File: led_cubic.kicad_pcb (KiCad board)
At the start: 2 copper layers, 100 x 100 mm, 82 parts, among them J1 Cathode Layer, Q1 2N2222, Q2 2N2222, Q3 2N2222, Q4 2N2222, U1 74HC595, U2 74HC595, U3 74HC595, U4 74HC595, U5 74HC595, U6 74HC595, U7 74HC595, U8 CORE-ESP32-C3-DevKit

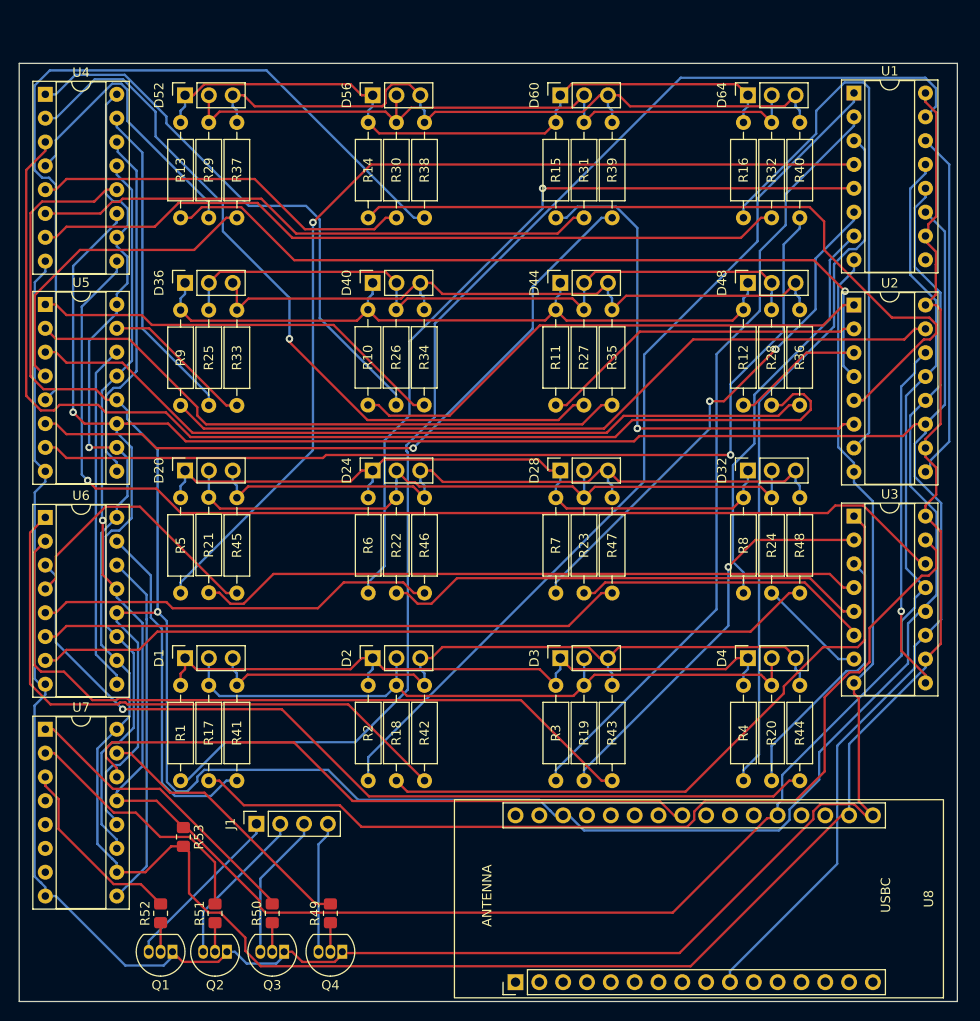
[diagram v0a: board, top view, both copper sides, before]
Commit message: 0.1.1
修改布局和PCB大小并添加M3螺丝孔
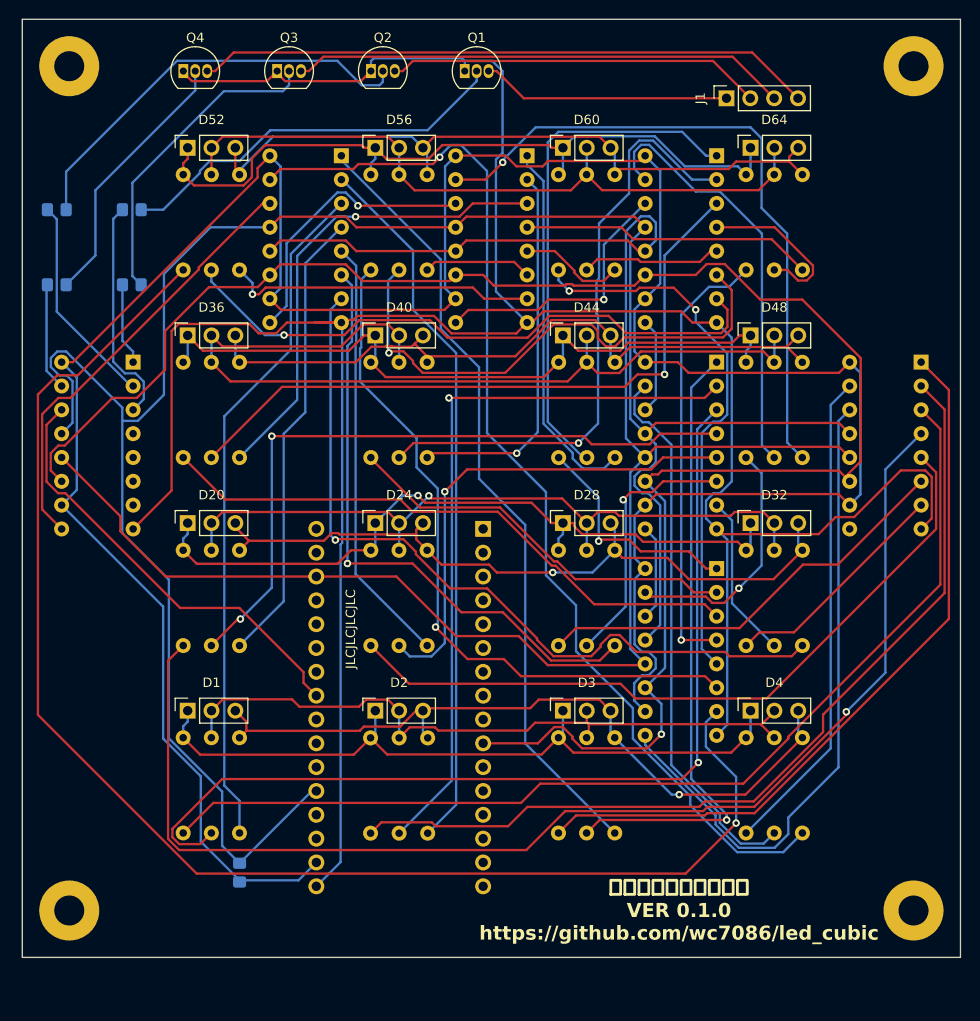
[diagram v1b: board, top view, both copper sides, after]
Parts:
- added P1: MountingHole_3.2mm_M3_Pad, MountingHole:MountingHole_3.2mm_M3_Pad, F.Cu at (183.4, 134.5)
- added P2: MountingHole_3.2mm_M3_Pad, MountingHole:MountingHole_3.2mm_M3_Pad, F.Cu at (93.4, 134.5)
- added P3: MountingHole_3.2mm_M3_Pad, MountingHole:MountingHole_3.2mm_M3_Pad, F.Cu at (93.4, 44.5)
- added P4: MountingHole_3.2mm_M3_Pad, MountingHole:MountingHole_3.2mm_M3_Pad, F.Cu at (183.4, 44.5)
- J1: footprint Connector_PinSocket_2.54mm:PinSocket_1x04_P2.54mm_Vertical -> Library:PinSocket_1x04_P2.54mm_Vertical
- R1, R10, R11, R12, R13, R14, R15, R16, R17, R18, R19, R2, R20, R21, R22, R23, R24, R25, R26, R27, R28, R29, R3, R30, R31, R32, R33, R34, R35, R36, R37, R38, R39, R4, R40, R41, R42, R43, R44, R45, R46, R47, R48, R49, R5, R50, R51, R52, R53, R6, R7, R8, R9, U8: moved to B.Cu
- U1, U2, U3, U4, U5, U6, U7: footprint Package_DIP:DIP-16_W7.62mm_Socket -> Library:DIP-16_W7.62mm_Socket; moved to B.Cu
- moved Q1 98.9 mm to (135.6, 45.1), turned to 0 degrees
- moved Q4 95.4 mm to (105.6, 45.1), turned to 0 degrees
- moved Q2 95.1 mm to (125.6, 45.1), turned to 0 degrees
- moved Q3 93.9 mm to (115.6, 45.1), turned to 0 degrees
- moved J1 92.2 mm to (163.5, 48.0)
- moved R51 76.9 mm to (92.1, 59.8), turned to 180 degrees
- moved R52 75.1 mm to (100.1, 59.8), turned to 180 degrees
- moved R49 73.1 mm to (92.1, 67.8), turned to 180 degrees
- moved R50 68.7 mm to (100.1, 67.8), turned to 180 degrees
- moved U4 68.0 mm to (158.6, 53.8), turned to 180 degrees
- moved R1 60.5 mm to (165.6, 116.1)
- moved R17 60.5 mm to (168.6, 116.1)
- moved R41 60.5 mm to (171.6, 116.1)
- moved R13 60.5 mm to (165.6, 56.1)
- moved R29 60.5 mm to (168.6, 56.1)
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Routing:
- net Net-(U3-SER): track 118.8 -> 10.2 mm, vias 1 -> 0
- net Net-(U2-QH): track 60.8 -> 152.5 mm, vias 0 -> 1
- net Net-(U1-QA): track 136.8 -> 52.2 mm
- net Net-(U6-QA): track 37.0 -> 117.3 mm, vias 0 -> 1
- net Net-(U3-QD): track 28.4 -> 103.3 mm, vias 0 -> 1
- net Net-(U5-QF): track 84.1 -> 11.3 mm
- net Net-(U5-QH): track 102.0 -> 33.2 mm
- net /P10: track 262.1 -> 194.2 mm
- net /P19: track 260.6 -> 192.9 mm, vias 1 -> 0
- net Net-(U5-QG): track 74.3 -> 11.6 mm, vias 1 -> 0
- net GND: track 237.3 -> 295.9 mm
- net Net-(U2-QA): track 84.8 -> 26.7 mm, vias 0 -> 1
- net Net-(U5-QA): track 16.2 -> 71.4 mm, vias 0 -> 1
- net /GND4: track 14.1 -> 65.8 mm
- net Net-(U2-QD): track 14.1 -> 63.9 mm
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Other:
- board text added: "JLCJLCJLCJLC"
- board text added: "陈基城，高鑫，覃远明 VER 0.1.0 https://github.com/wc7086/led_cubic"

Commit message: 0.1.2
调整 LED 插座焊盘间距，修改布局，重新布线
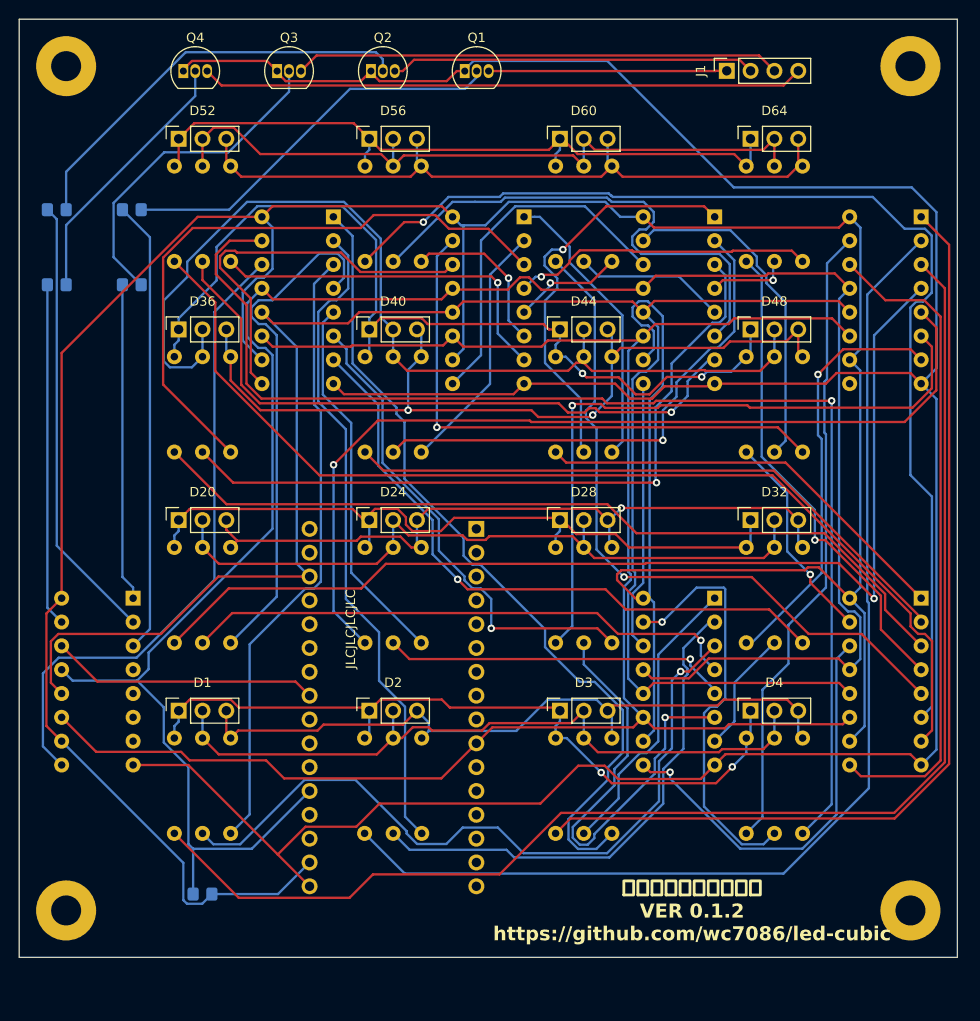
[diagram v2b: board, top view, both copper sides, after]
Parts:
- moved U3 25.2 mm to (158.4, 100.9)
- moved U7 25.2 mm to (96.4, 100.9)
- moved U2 22.0 mm to (180.4, 100.9)
- moved U1 15.5 mm to (180.4, 60.3)
- moved U6 6.57 mm to (117.8, 60.3)
- moved U5 6.52 mm to (138.1, 60.3)
- moved U4 6.51 mm to (158.4, 60.3)
- moved R53 4.57 mm to (107.6, 132.8), turned to 0 degrees
- moved J1 2.93 mm to (163.5, 45.0)
- moved D52 1.36 mm to (105.1, 52.3)
- moved R16 1.31 mm to (104.6, 55.2)
- moved R32 1.31 mm to (107.6, 55.2)
- moved R40 1.31 mm to (110.6, 55.2)
- moved D36 1.15 mm to (105.1, 72.6)
- moved D56 1.15 mm to (125.4, 52.3)
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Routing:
- net +5V: track 292.4 -> 356.1 mm
- net Net-(U2-QG): track 74.7 -> 119.4 mm
- net Net-(U2-QH): track 152.5 -> 113.8 mm, vias 1 -> 0
- net Net-(U3-QB): track 67.0 -> 31.3 mm, vias 1 -> 0
- net Net-(U2-SER): track 10.2 -> 44.8 mm, vias 0 -> 1
- net Net-(U1-QD): track 111.3 -> 145.1 mm
- net Net-(U1-QG): track 45.9 -> 71.7 mm, vias 0 -> 1
- net Net-(U2-QD): track 63.9 -> 89.2 mm
- net Net-(U7-QB): track 8.72 -> 33.9 mm
- net Net-(U7-QA): track 11.5 -> 36.6 mm
- net Net-(U7-QC): track 22.7 -> 47.7 mm
- net Net-(U1-QB): track 79.7 -> 104.6 mm
- net Net-(U3-QD): track 103.3 -> 78.7 mm
- net Net-(U7-QD): track 24.2 -> 48.4 mm
- net Net-(U2-QC): track 42.9 -> 67.0 mm
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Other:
- board text added: "陈基城，高鑫，覃远明 VER 0.1.2 https://github.com/wc7086/led-cubic"
- board text removed: "陈基城，高鑫，覃远明 VER 0.1.0 https://github.com/wc7086/led_cubic"

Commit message: 修复PCB，删除每排LED的并联线路
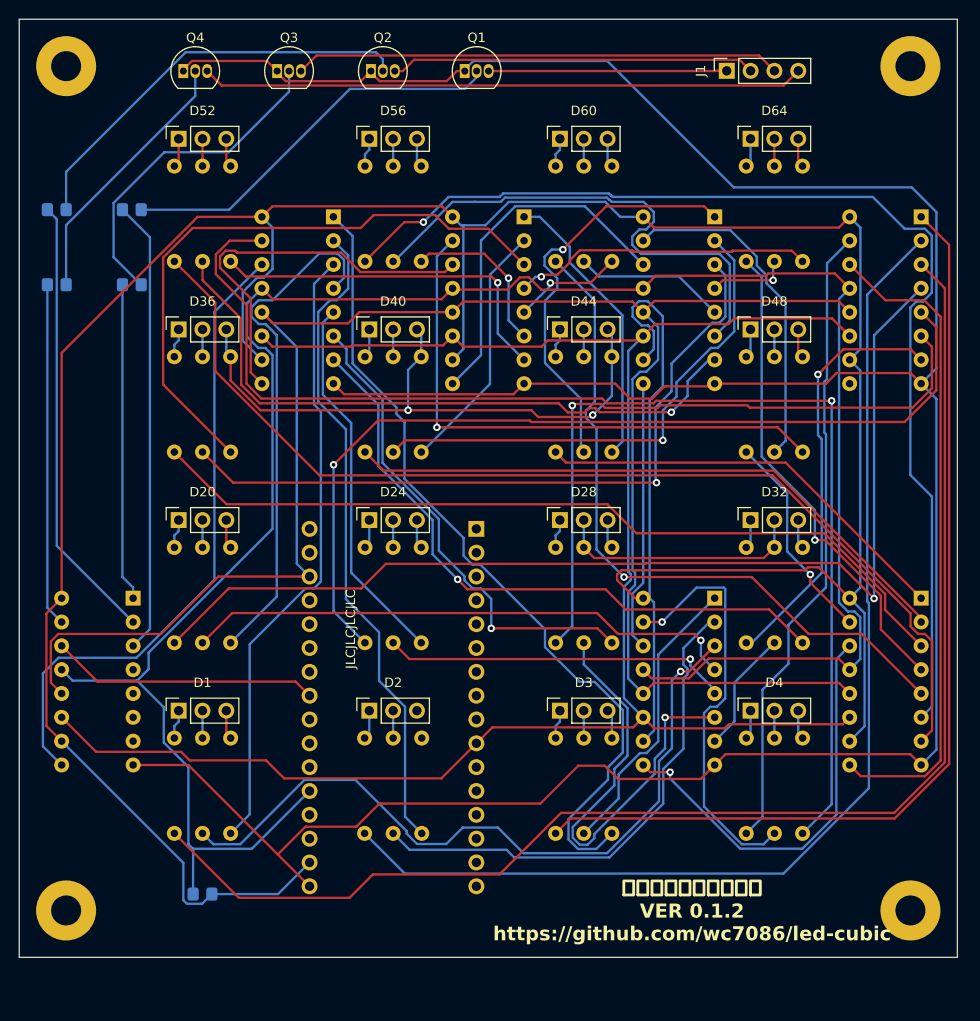
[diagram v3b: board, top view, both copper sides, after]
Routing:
- net /G3: track 106.6 -> 11.6 mm
- net /B3: track 98.0 -> 12.4 mm, vias 2 -> 0
- net /B1: track 80.9 -> 13.0 mm, vias 2 -> 0
- net /R1: track 76.4 -> 9.33 mm
- net /B2: track 78.3 -> 12.4 mm
- net /G1: track 76.8 -> 11.7 mm
- net /G4: track 76.7 -> 11.6 mm
- net /B4: track 76.5 -> 12.4 mm
- net /R4: track 76.0 -> 12.4 mm
- net /R2: track 75.9 -> 12.4 mm, vias 1 -> 0
- net /G2: track 76.6 -> 32.9 mm
- net /R3: track 89.6 -> 68.6 mm
